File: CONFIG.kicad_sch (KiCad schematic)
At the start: 23 parts, among them IC1 ECP5-BGA256, J1 Conn_ARM_JTAG_SWD_10, U5 AT25SF081-SSHD-X

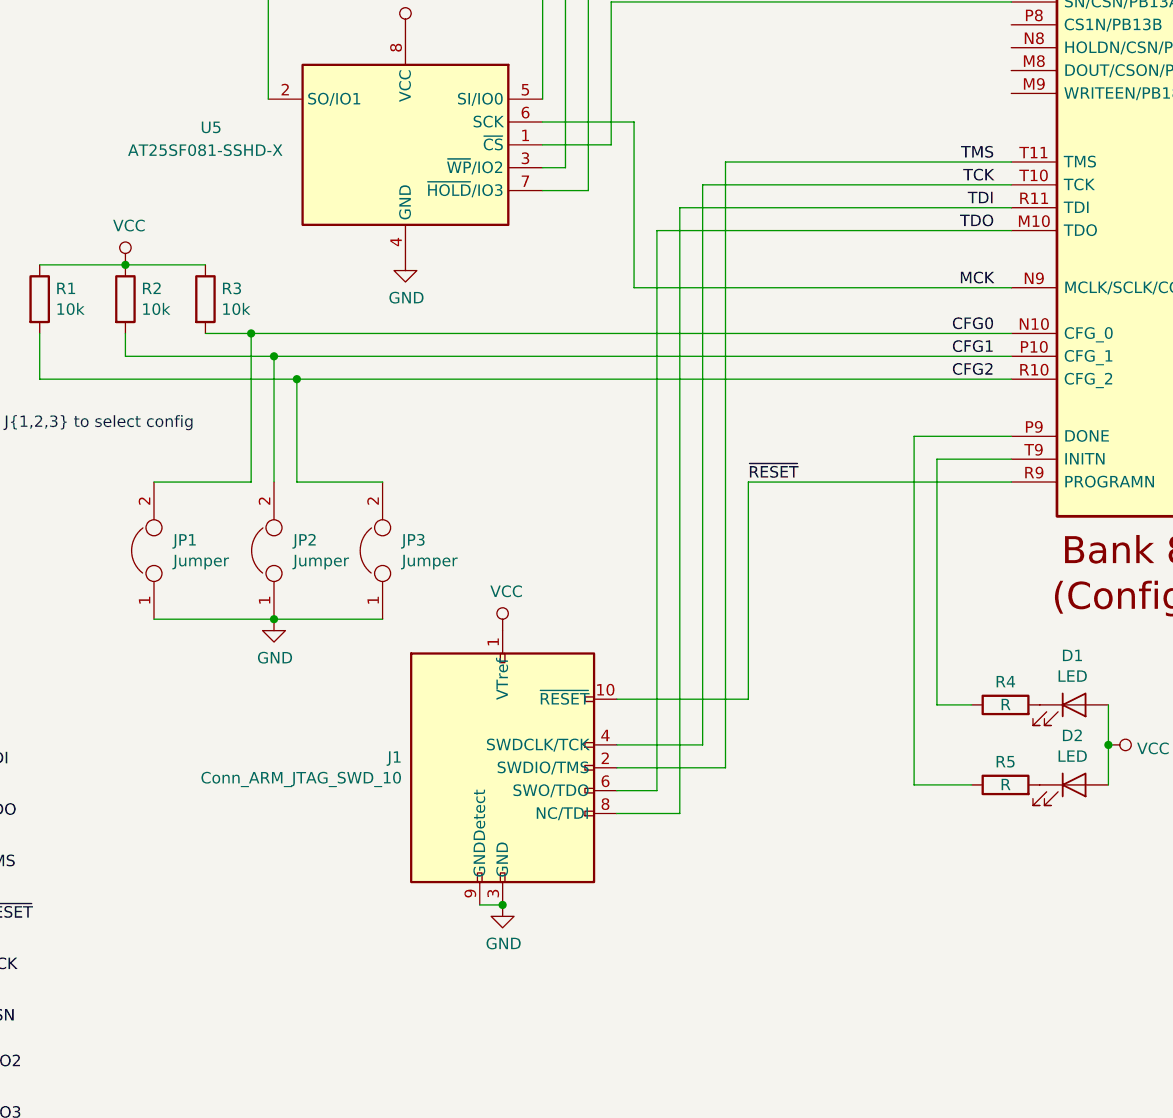
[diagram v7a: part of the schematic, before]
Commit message: Change debug header to 2.54mm standard
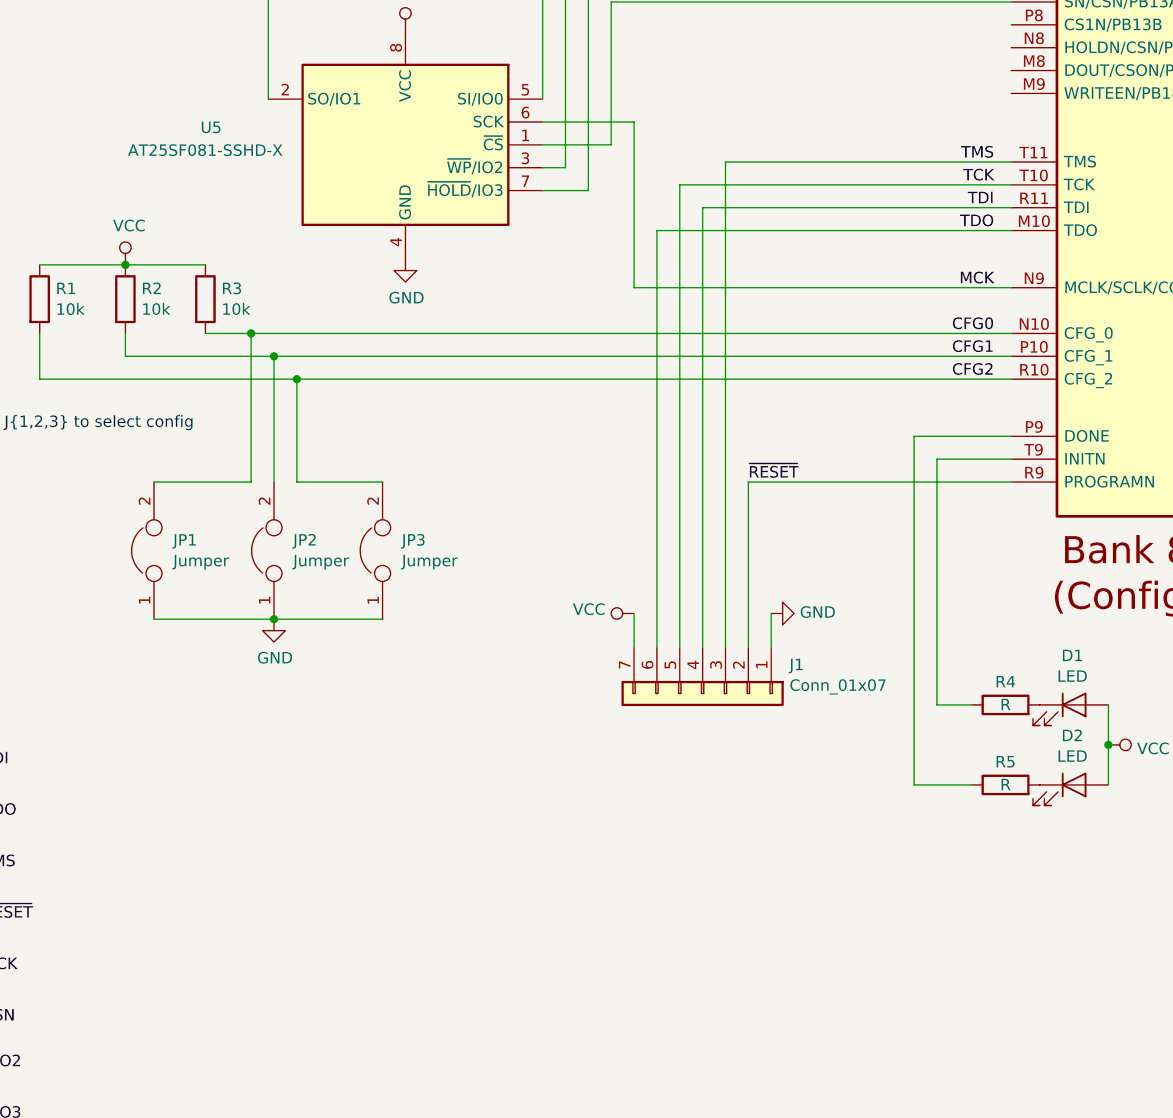
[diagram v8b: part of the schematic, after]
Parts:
- removed J1: Conn_ARM_JTAG_SWD_10, Connector:Tag-Connect_TC2050-IDC-NL_2x05_P1.27mm_Vertical, symbol Connector:Conn_ARM_JTAG_SWD_10
- added J1: Conn_01x07, Connector_PinHeader_2.54mm:PinHeader_1x07_P2.54mm_Vertical, symbol Connector_Generic:Conn_01x07
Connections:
- net GND: now also J1.1 (Pin_1)
- net TCK: now also J1.5 (Pin_5)
- net TDI: now also J1.4 (Pin_4)
- net TDO: now also J1.6 (Pin_6)
- net TMS: now also J1.3 (Pin_3)
- net VCC: now also J1.7 (Pin_7)
- net ~RESET: now also J1.2 (Pin_2)
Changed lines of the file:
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@@
-(kicad_sch (version 20200714) (host eeschema "5.99.0-unknown-a61ea1f~102~ubuntu20.04.1")
+(kicad_sch (version 20200714) (host eeschema "5.99.0-unknown-8324cb3~102~ubuntu20.04.1")
   (page 4 6)
   (paper "A4")
@@
   (junction (at 132.715 124.46) (diameter 0) (color 0 0 0 0))
   (junction (at 135.255 97.79) (diameter 0) (color 0 0 0 0))
-  (junction (at 158.115 156.21) (diameter 0) (color 0 0 0 0))
   (junction (at 225.425 138.43) (diameter 0) (color 0 0 0 0))
   (junction (at 236.22 19.05) (diameter 0) (color 0 0 0 0))
@@
     (stroke (width 0) (type solid) (color 0 0 0 0))
   )
-  (wire (pts (xy 155.575 156.21) (xy 158.115 156.21))
-    (stroke (width 0) (type solid) (color 0 0 0 0))
-  )
   (wire (pts (xy 162.56 53.34) (xy 162.56 66.675))
     (stroke (width 0) (type solid) (color 0 0 0 0))
@@
     (stroke (width 0) (type solid) (color 0 0 0 0))
   )
-  (wire (pts (xy 170.815 133.35) (xy 185.42 133.35))
-    (stroke (width 0) (type solid) (color 0 0 0 0))
-  )
-  (wire (pts (xy 170.815 138.43) (xy 180.34 138.43))
-    (stroke (width 0) (type solid) (color 0 0 0 0))
-  )
-  (wire (pts (xy 170.815 140.97) (xy 182.88 140.97))
-    (stroke (width 0) (type solid) (color 0 0 0 0))
-  )
-  (wire (pts (xy 170.815 143.51) (xy 175.26 143.51))
-    (stroke (width 0) (type solid) (color 0 0 0 0))
-  )
-  (wire (pts (xy 170.815 146.05) (xy 177.8 146.05))
-    (stroke (width 0) (type solid) (color 0 0 0 0))
-  )
   (wire (pts (xy 172.72 69.215) (xy 162.56 69.215))
     (stroke (width 0) (type solid) (color 0 0 0 0))
@@
     (stroke (width 0) (type solid) (color 0 0 0 0))
   )
-  (wire (pts (xy 175.26 81.28) (xy 214.63 81.28))
-    (stroke (width 0) (type solid) (color 0 0 0 0))
-  )
-  (wire (pts (xy 175.26 143.51) (xy 175.26 81.28))
-    (stroke (width 0) (type solid) (color 0 0 0 0))
-  )
-  (wire (pts (xy 177.8 78.74) (xy 214.63 78.74))
-    (stroke (width 0) (type solid) (color 0 0 0 0))
-  )
-  (wire (pts (xy 177.8 146.05) (xy 177.8 78.74))
-    (stroke (width 0) (type solid) (color 0 0 0 0))
-  )
-  (wire (pts (xy 180.34 76.2) (xy 214.63 76.2))
-    (stroke (width 0) (type solid) (color 0 0 0 0))
-  )
-  (wire (pts (xy 180.34 138.43) (xy 180.34 76.2))
+  (wire (pts (xy 172.72 123.825) (xy 172.72 127.635))
+    (stroke (width 0) (type solid) (color 0 0 0 0))
+  )
+  (wire (pts (xy 175.26 81.28) (xy 175.26 127.635))
+    (stroke (width 0) (type solid) (color 0 0 0 0))
+  )
+  (wire (pts (xy 177.8 76.2) (xy 177.8 127.635))
+    (stroke (width 0) (type solid) (color 0 0 0 0))
+  )
+  (wire (pts (xy 177.8 76.2) (xy 214.63 76.2))
+    (stroke (width 0) (type solid) (color 0 0 0 0))
+  )
+  (wire (pts (xy 180.34 78.74) (xy 180.34 127.635))
+    (stroke (width 0) (type solid) (color 0 0 0 0))
+  )
+  (wire (pts (xy 180.34 78.74) (xy 214.63 78.74))
+    (stroke (width 0) (type solid) (color 0 0 0 0))
+  )
+  (wire (pts (xy 182.88 73.66) (xy 182.88 127.635))
     (stroke (width 0) (type solid) (color 0 0 0 0))
   )
@@
     (stroke (width 0) (type solid) (color 0 0 0 0))
   )
-  (wire (pts (xy 182.88 140.97) (xy 182.88 73.66))
-    (stroke (width 0) (type solid) (color 0 0 0 0))
-  )
-  (wire (pts (xy 185.42 109.22) (xy 185.42 133.35))
+  (wire (pts (xy 185.42 109.22) (xy 185.42 127.635))
     (stroke (width 0) (type solid) (color 0 0 0 0))
   )
@@
     (stroke (width 0) (type solid) (color 0 0 0 0))
   )
+  (wire (pts (xy 187.96 123.825) (xy 187.96 127.635))
+    (stroke (width 0) (type solid) (color 0 0 0 0))
+  )
   (wire (pts (xy 203.835 104.14) (xy 214.63 104.14))
     (stroke (width 0) (type solid) (color 0 0 0 0))
@@
   )
   (wire (pts (xy 206.375 133.985) (xy 210.185 133.985))
+    (stroke (width 0) (type solid) (color 0 0 0 0))
+  )
+  (wire (pts (xy 214.63 81.28) (xy 175.26 81.28))
     (stroke (width 0) (type solid) (color 0 0 0 0))
   )
@@
     )
   )
-  (symbol (lib_id "power:VCC") (at 158.115 125.73 0) (unit 1)
-    (in_bom yes) (on_board yes)
-    (property "Reference" "#PWR0124" (id 0) (at 158.115 129.54 0)
-      (effects (font (size 1.27 1.27)) hide)
-    )
-    (property "Value" "VCC" (id 1) (at 158.5468 121.4056 0))
-    (property "Footprint" "" (id 2) (at 158.115 125.73 0)
-      (effects (font (size 1.27 1.27)) hide)
-    )
-    (property "Datasheet" "" (id 3) (at 158.115 125.73 0)
+  (symbol (lib_id "power:VCC") (at 172.72 123.825 90) (unit 1)
+    (in_bom yes) (on_board yes)
+    (property "Reference" "#PWR0126" (id 0) (at 176.53 123.825 0)
+      (effects (font (size 1.27 1.27)) hide)
+    )
+    (property "Value" "VCC" (id 1) (at 169.5449 123.3932 90)
+      (effects (font (size 1.27 1.27)) (justify left))
+    )
+    (property "Footprint" "" (id 2) (at 172.72 123.825 0)
+      (effects (font (size 1.27 1.27)) hide)
+    )
+    (property "Datasheet" "" (id 3) (at 172.72 123.825 0)
       (effects (font (size 1.27 1.27)) hide)
     )
@@
     )
   )
-  (symbol (lib_id "power:GND") (at 158.115 156.21 0) (unit 1)
-    (in_bom yes) (on_board yes)
-    (property "Reference" "#PWR0126" (id 0) (at 158.115 162.56 0)
-      (effects (font (size 1.27 1.27)) hide)
-    )
-    (property "Value" "GND" (id 1) (at 158.2293 160.5344 0))
-    (property "Footprint" "" (id 2) (at 158.115 156.21 0)
-      (effects (font (size 1.27 1.27)) hide)
-    )
-    (property "Datasheet" "" (id 3) (at 158.115 156.21 0)
+  (symbol (lib_id "power:GND") (at 187.96 123.825 90) (unit 1)
+    (in_bom yes) (on_board yes)
+    (property "Reference" "#PWR0124" (id 0) (at 194.31 123.825 0)
+      (effects (font (size 1.27 1.27)) hide)
+    )
+    (property "Value" "GND" (id 1) (at 191.1351 123.7107 90)
+      (effects (font (size 1.27 1.27)) (justify right))
+    )
+    (property "Footprint" "" (id 2) (at 187.96 123.825 0)
+      (effects (font (size 1.27 1.27)) hide)
+    )
+    (property "Datasheet" "" (id 3) (at 187.96 123.825 0)
       (effects (font (size 1.27 1.27)) hide)
     )
@@
     )
   )
-  (symbol (lib_id "Connector:Conn_ARM_JTAG_SWD_10") (at 158.115 140.97 0) (unit 1)
-    (in_bom yes) (on_board yes)
-    (property "Reference" "J1" (id 0) (at 146.9389 139.8206 0)
-      (effects (font (size 1.27 1.27)) (justify right))
-    )
-    (property "Value" "Conn_ARM_JTAG_SWD_10" (id 1) (at 146.9389 142.1193 0)
-      (effects (font (size 1.27 1.27)) (justify right))
-    )
-    (property "Footprint" "Connector:Tag-Connect_TC2050-IDC-NL_2x05_P1.27mm_Vertical" (id 2) (at 158.115 140.97 0)
-      (effects (font (size 1.27 1.27)) hide)
-    )
-    (property "Datasheet" "http://infocenter.arm.com/help/topic/com.arm.doc.ddi0314h/DDI0314H_coresight_components_trm.pdf" (id 3) (at 149.225 172.72 90)
-      (effects (font (size 1.27 1.27)) hide)
-    )
+  (symbol (lib_id "Connector_Generic:Conn_01x07") (at 180.34 132.715 270) (unit 1)
+    (in_bom yes) (on_board yes)
+    (property "Reference" "J1" (id 0) (at 189.9921 129.5336 90)
+      (effects (font (size 1.27 1.27)) (justify left))
+    )
+    (property "Value" "Conn_01x07" (id 1) (at 189.9921 131.8323 90)
+      (effects (font (size 1.27 1.27)) (justify left))
+    )
+    (property "Footprint" "Connector_PinHeader_2.54mm:PinHeader_1x07_P2.54mm_Vertical" (id 2) (at 180.34 132.715 0)
+      (effects (font (size 1.27 1.27)) hide)
+    )
+    (property "Datasheet" "~" (id 3) (at 180.34 132.715 0)
+      (effects (font (size 1.27 1.27)) hide)
+    )
